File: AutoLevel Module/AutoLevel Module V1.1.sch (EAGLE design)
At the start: 10 parts

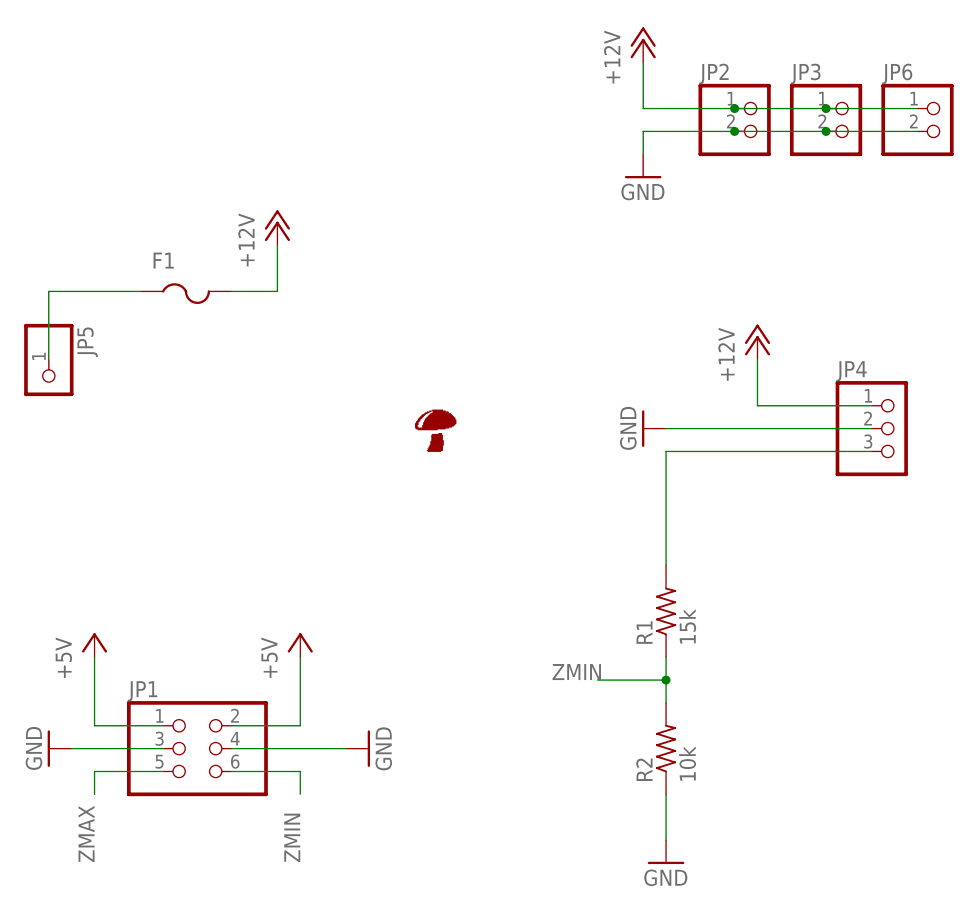
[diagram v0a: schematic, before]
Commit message: Ordered new AL boards
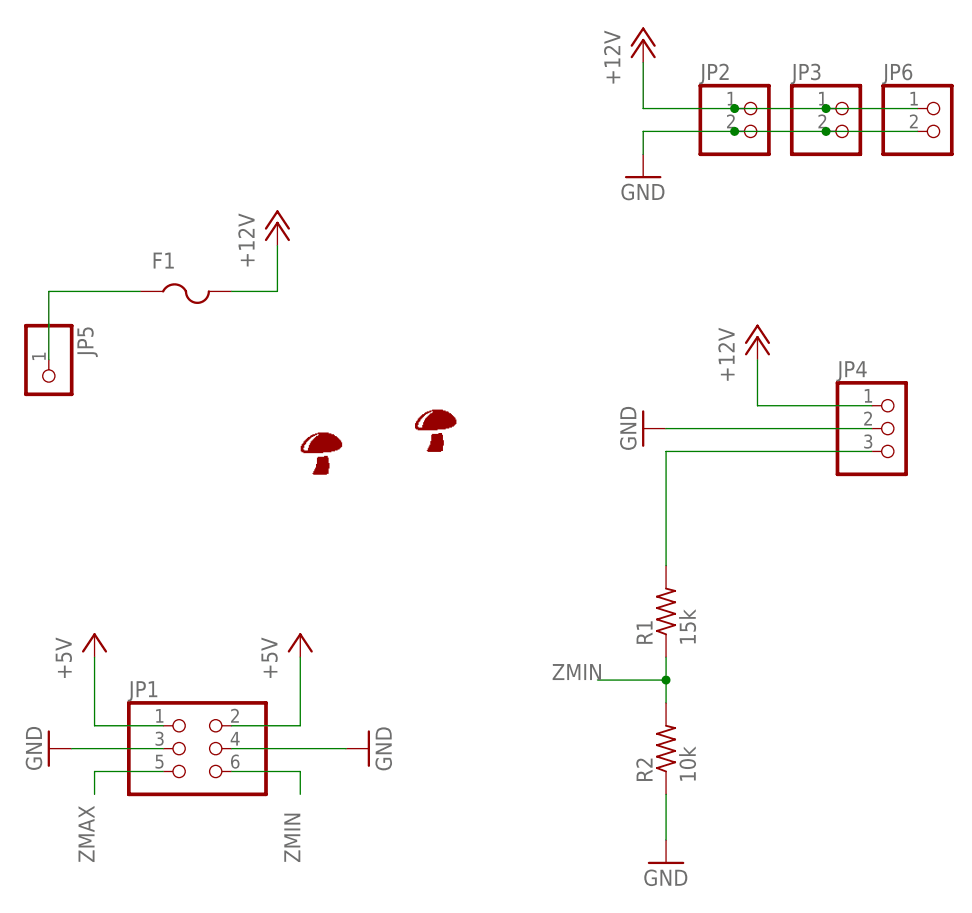
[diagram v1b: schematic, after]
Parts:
- added U$2: SHROOMBOTTOMSILK, RobThePyro:SHROOMBOTTOMSILK
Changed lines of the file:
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@@
 <?xml version="1.0" encoding="utf-8"?>
 <!DOCTYPE eagle SYSTEM "eagle.dtd">
-<eagle version="7.3.0">
+<eagle version="8.0.2">
 <drawing>
 <settings>
@@
 <part name="JP6" library="pinhead" deviceset="PINHD-1X2" device=""/>
 <part name="U$1" library="RobThePyro" deviceset="SHROOM" device="5MM"/>
+<part name="U$2" library="RobThePyro" deviceset="SHROOM" device="BOTTOMSILK"/>
 </parts>
 <sheets>
@@
 <instance part="JP6" gate="G$1" x="127" y="129.54"/>
 <instance part="U$1" gate="G$1" x="68.58" y="93.98"/>
+<instance part="U$2" gate="G$1" x="55.88" y="91.44"/>
 </instances>
 <busses>
